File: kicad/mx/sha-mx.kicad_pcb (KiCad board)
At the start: 2 copper layers, 266 x 76 mm, 111 parts, among them SW1 SW_Push, SW10 SW_Push, SW11 SW_Push, SW12 SW_Push, SW13 SW_Push, SW14 SW_Push, SW15 SW_Push, SW16 SW_Push, SW17 SW_Push, SW18 SW_Push, SW19 SW_Push, SW2 SW_Push, SW20 SW_Push, SW21 SW_Push, SW22 SW_Push, SW23 SW_Push, SW24 SW_Push, SW25 SW_Push, SW26 SW_Push, SW27 SW_Push, SW28 SW_Push, SW29 SW_Push, SW3 SW_Push, SW30 SW_Push, SW31 SW_Push, SW32 SW_Push, SW33 SW_Push, SW34 SW_Push, SW35 SW_Push, SW36 SW_Push, SW37 SW_Push, SW38 SW_Push, SW39 SW_Push, SW4 SW_Push, SW40 SW_Push, SW41 SW_Push, SW42 SW_Push, SW43 SW_Push, SW44 SW_Push, SW45 SW_Push, SW46 SW_Push, SW47 SW_Push, SW48 SW_Push, SW49 SW_Push, SW5 SW_Push, SW50 SW_Push, SW6 SW_Push, SW7 SW_Push, SW8 SW_Push, SW9 SW_Push, U1 RP2040-Zero

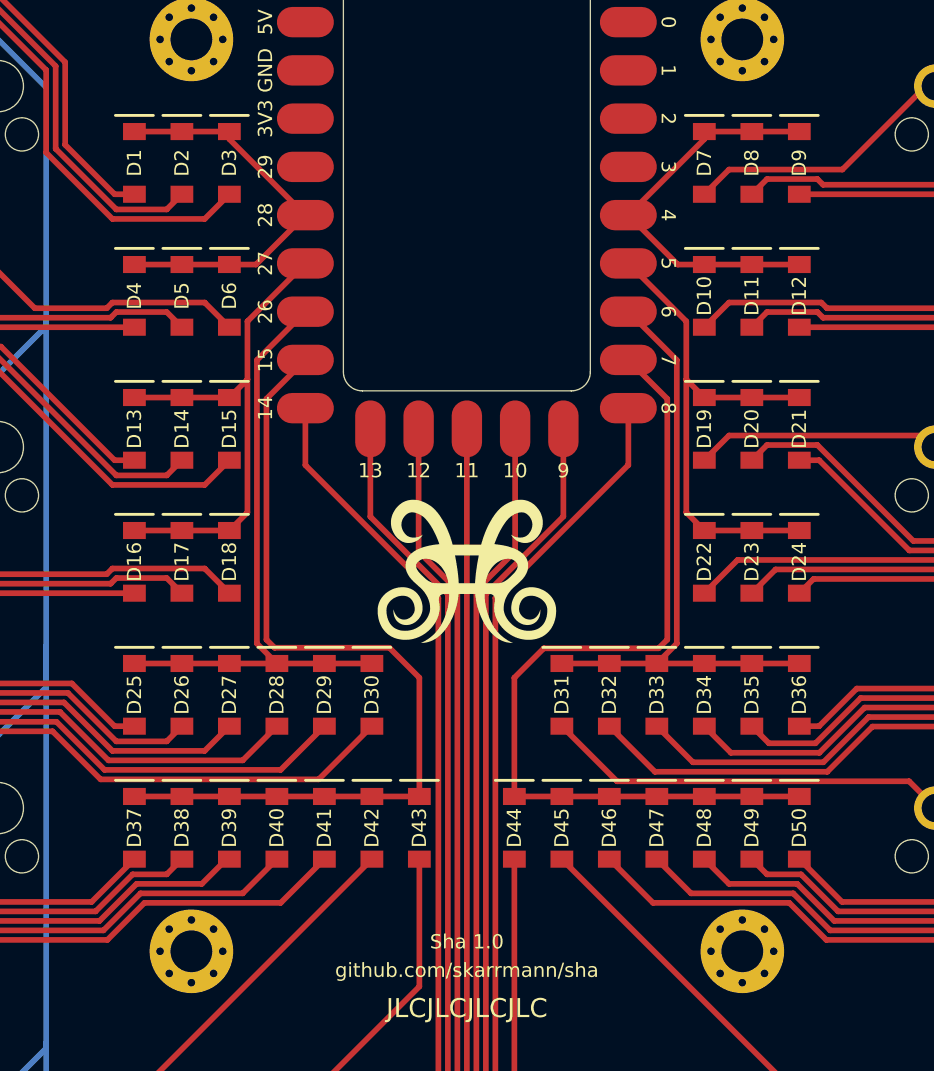
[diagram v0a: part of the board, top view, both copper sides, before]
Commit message: Create Choc switch design, update logos
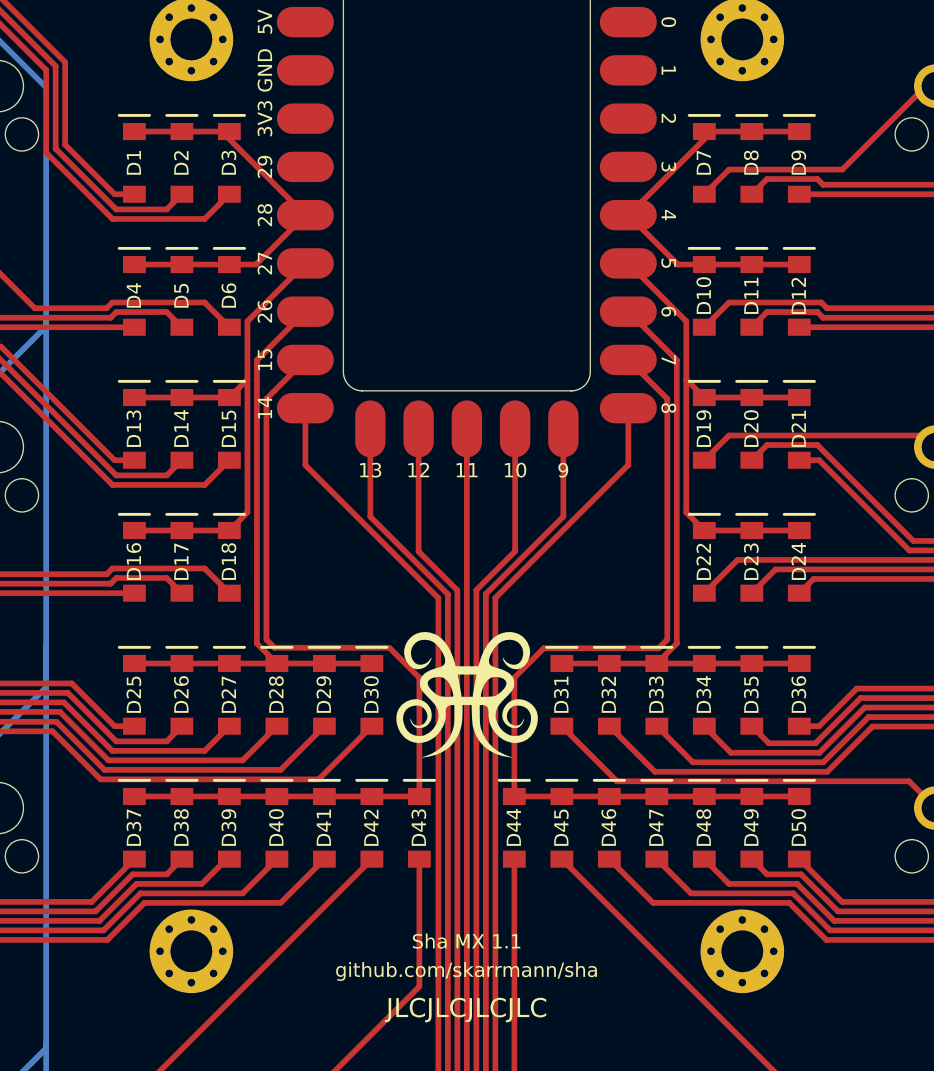
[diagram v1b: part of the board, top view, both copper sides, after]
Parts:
- moved LOGO2 6.50 mm to (148.5, 94.5)
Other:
- board text added: "Sha MX 1.1"
- board text removed: "Sha 1.0"
